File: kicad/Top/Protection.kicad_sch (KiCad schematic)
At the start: 17 parts

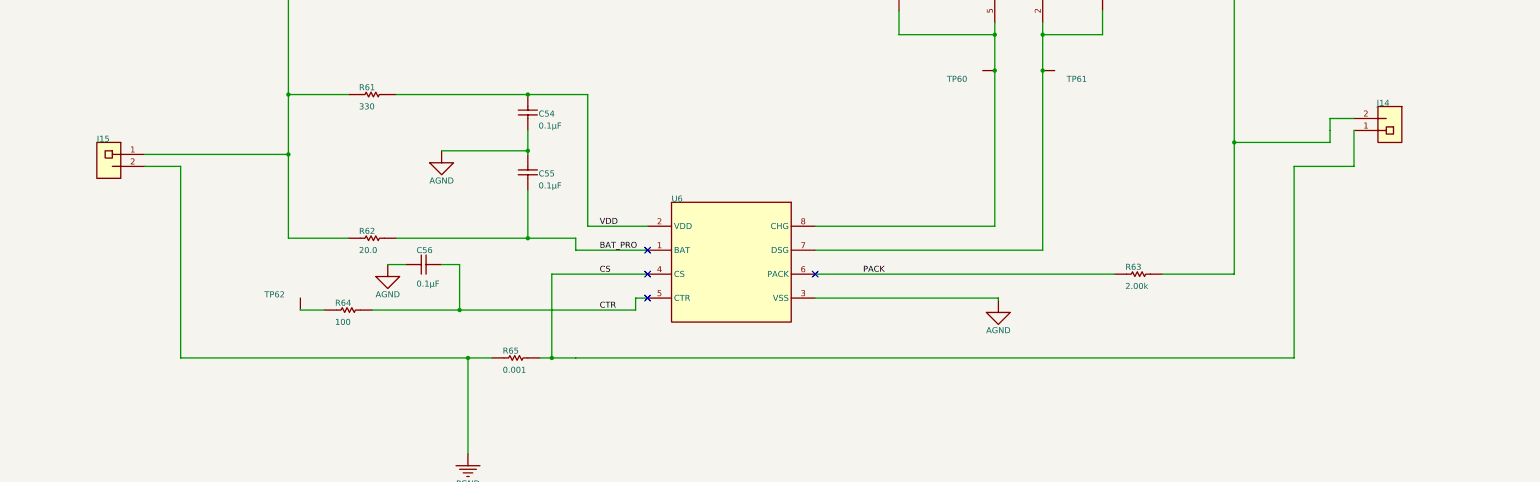
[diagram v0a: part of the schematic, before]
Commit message: Properly synced pcb to schematic
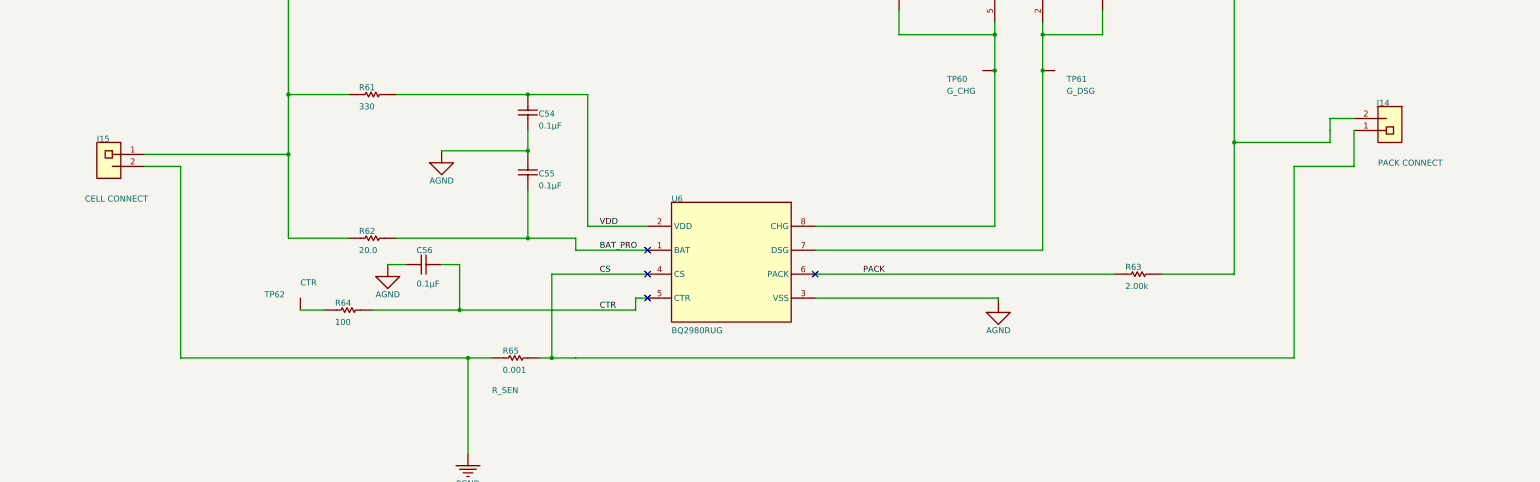
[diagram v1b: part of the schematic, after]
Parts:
- C54, C55, C56: value ~ -> GRM188R71H104KA93D; footprint 0603L -> AltiumImports:0603L
- J14: value ~ -> PACK CONNECT; footprint TERM_BLK_ED555-2DS -> AltiumImports:TERM_BLK_ED555-2DS
- J15: value ~ -> CELL CONNECT; footprint TERM_BLK_ED555-2DS -> AltiumImports:TERM_BLK_ED555-2DS
- R59, R60: value ~ -> CRCW04025M10JNED; footprint 0402L -> AltiumImports:0402L
- R61: value ~ -> CRCW0402330RJNED; footprint 0402L -> AltiumImports:0402L
- R62: value ~ -> CRCW040220R0FKED; footprint 0402L -> AltiumImports:0402L
- R63: value ~ -> CRCW04022K00FKED; footprint 0402L -> AltiumImports:0402L
- R64: value ~ -> CRCW0402100RFKED; footprint 0402L -> AltiumImports:0402L
- R65: value ~ -> R_SEN; footprint 1206 -> AltiumImports:1206
- TP60: value ~ -> G_CHG; footprint TESTPOINT -> AltiumImports:TESTPOINT
- TP61: value ~ -> G_DSG; footprint TESTPOINT -> AltiumImports:TESTPOINT
- TP62: value ~ -> CTR; footprint Keystone5012 -> AltiumImports:Keystone5012
- U5: value ~ -> EFC8811R-TF; footprint CSP6_568AL -> AltiumImports:CSP6_568AL
- U6: value ~ -> BQ2980RUG; footprint RUG0008A -> AltiumImports:RUG0008A
